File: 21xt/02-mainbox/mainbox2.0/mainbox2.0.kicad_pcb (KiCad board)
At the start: 2 copper layers, 65 parts, among them IC1 AD7175-8BCPZ-RL7, IC2 XBP9X-DMUS-011, J1 Conn_01x10, J10 Conn_02x20_Odd_Even, J3 Conn_01x06, J4 Conn_01x06, J6 Conn_01x02, J7 Conn_01x02, J9 Conn_01x06, U1 AD8222ACPZ-R7, U2 TPS78326DDCT, U3 LT6658AHMSE-2.5-PBF, U4 LT6658AHMSE-5-PBF, U5 SN74LVC245AN

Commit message: sophie needs to fix this
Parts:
- removed J6: Conn_01x02, Connector_PinHeader_2.54mm:PinHeader_1x02_P2.54mm_Vertical
- added REF**: DSUB-44-HD_Female_Horizontal_P2.29x1.98mm_EdgePinOffset3.03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, Connector_Dsub:DSUB-44-HD_Female_Horizontal_P2.29x1.98mm_EdgePinOffset3.03mm_Housed_MountingHolesOffset4.94mm, F.Cu at (20.9, 35.8)
- C1: footprint 21xt_footprints:R78B5015L - -> Capacitor_SMD:C_0603_1608Metric
- IC2: moved to B.Cu
- PS1: footprint 21xt_footprints:R78B5015L - -> 21xt_footprints:CONV_R-78B3.3-1.5
- moved C22 171.4 mm to (218.7, 71.2)
- moved C21 170.6 mm to (216.4, 97.5)
- moved C20 170.1 mm to (213.4, 98.8)
- moved C19 160.9 mm to (215.4, 73.2)
- moved C18 157.2 mm to (210.3, 84.1)
- moved C15 155.6 mm to (201.2, 84.1)
- moved C14 155.1 mm to (198.1, 84.1)
- moved C16 154.5 mm to (200.9, 69.6), turned to -90 degrees
- moved C17 151.7 mm to (201.2, 73.4)
- moved C23 151.5 mm to (202.2, 99.8)
- moved C24 145.8 mm to (199.1, 97.3)
- moved C31 140.3 mm to (183.5, 10.5), turned to 0 degrees
- moved R4 128.7 mm to (183.5, 23.2), turned to 180 degrees
- moved IC2 112.7 mm to (13.5, 135.3), turned to 180 degrees
- moved IC1 102.5 mm to (51.8, 28.2)
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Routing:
- added copper zone on F.Cu, net (none)
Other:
- copper layers 2 -> 4

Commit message: 3D modeled
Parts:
- removed REF**: DSUB-44-HD_Female_Horizontal_P2.29x1.98mm_EdgePinOffset3.03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, Connector_Dsub:DSUB-44-HD_Female_Horizontal_P2.29x1.98mm_EdgePinOffset3.03mm_Housed_MountingHolesOffset4.94mm
- moved C20 89.0 mm to (127.0, 77.4)
- moved C21 89.0 mm to (130.0, 76.1)
- moved C23 89.0 mm to (115.8, 78.4)
- moved C24 89.0 mm to (112.8, 75.9)
- moved U4 89.0 mm to (121.3, 75.7)
- moved J1 61.5 mm to (94.5, 56.9), turned to 90 degrees
- moved IC2 59.5 mm to (12.1, 75.8)
- moved C17 59.4 mm to (142.0, 68.4)
- moved C16 59.4 mm to (141.7, 64.6)
- moved C19 59.4 mm to (156.2, 68.1)
- moved C22 59.4 mm to (159.5, 66.1)
- moved U3 59.4 mm to (148.4, 66.6)
- moved J9 56.6 mm to (152.8, 48.8)
- moved J3 55.9 mm to (227.5, 41.1)
- moved C18 51.9 mm to (158.9, 77.3)
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
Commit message: progress
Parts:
- removed C11, C12, C13: 0.1uF, Capacitor_SMD:C_0603_1608Metric
- removed J4: Conn_01x06, 21xt_footprints:CONN_S6B-PH-K-S_JST (1x6)
- removed J7: Conn_01x02, Connector_PinHeader_2.54mm:PinHeader_1x02_P2.54mm_Vertical
- removed J9: Conn_01x06, 21xt_footprints:MOLEX_0533980671 (1x6)
- removed R4: 10k, Resistor_SMD:R_0603_1608Metric
- removed TP1, TP2, TP3, TP4, TP5, TP6, TP7: TestPoint, TestPoint:TestPoint_Pad_1.5x1.5mm
- removed U2: TPS78326DDCT, 21xt_footprints:TPS78326DDCT
- removed U3: LT6658AHMSE-2.5-PBF, 21xt_footprints:LT6658AHMSE-2.5-PBF
- removed U5: SN74LVC245AN, 21xt_footprints:SN74LVC245AN
- added C32: 0.1uF, Capacitor_SMD:C_0603_1608Metric, F.Cu at (100.1, 67.7)
- added C33: 3.3uF, Capacitor_SMD:C_0603_1608Metric, F.Cu at (103.1, 62.0)
- added C34: 1uF, Capacitor_SMD:C_0603_1608Metric, F.Cu at (108.4, 69.3)
- added C35: 47uF, Capacitor_SMD:C_0603_1608Metric, F.Cu at (110.2, 69.3)
- added C36: 10uF, Capacitor_SMD:C_0603_1608Metric, F.Cu at (155.6, 47.0)
- added C37: 10uF, Capacitor_SMD:C_0603_1608Metric, F.Cu at (153.7, 47.1)
- added C39: 15pF, Capacitor_SMD:C_0603_1608Metric, F.Cu at (151.7, 52.8)
- added C40: 10uF, Capacitor_SMD:C_0603_1608Metric, F.Cu at (145.5, 53.9)
- added C41: 10uF, Capacitor_SMD:C_0603_1608Metric, F.Cu at (145.5, 52.2)
- added C42: 10uF, Capacitor_SMD:C_0603_1608Metric, F.Cu at (145.5, 50.6)
- added C43: 10uF, Capacitor_SMD:C_0603_1608Metric, F.Cu at (145.5, 48.9)
- added C44: 0.1uF, Capacitor_SMD:C_0603_1608Metric, F.Cu at (133.0, 88.8)
- added C45: 0.1uF, Capacitor_SMD:C_0603_1608Metric, F.Cu at (140.3, 84.2)
- added C46: 0.1uF, Capacitor_SMD:C_0603_1608Metric, F.Cu at (140.6, 88.8)
- added IC3: TPS61088QRHLTQ1, 21xt_footprints:BQ24123RHLT, F.Cu at (104.2, 68.1)
- added IC6: AP3441LSHE-7B, 21xt_footprints:AP3441LSHE7B, F.Cu at (150.2, 48.8)
- added IC7: SN74LVC2T45DCTTG4, 21xt_footprints:SOP65P400X130-8N, F.Cu at (136.5, 84.2)
- added IC8: SN74LVC2T45DCTTG4, 21xt_footprints:SOP65P400X130-8N, F.Cu at (136.8, 88.8)
- added J2: Conn_01x10, 21xt_footprints:908160010(picolex-10), F.Cu at (91.5, 68.7)
- added J5: MDT275M02001, 21xt_footprints:AMPHENOL_MDT275M02001, F.Cu at (155.2, 69.1)
- added J6: Conn_01x02, 21xt_footprints:JST_B2P-VH_LF__SN_(2 pin), F.Cu at (95.2, 47.2)
- added L2: 22uH, Inductor_SMD:L_0402_1005Metric, F.Cu at (148.4, 45.1)
- added L3: 1.2uH, Inductor_SMD:L_0402_1005Metric, F.Cu at (98.5, 67.7)
- added Q1: DMG1012T-7, 21xt_footprints:SOT50P160X90-3N(DIODE), F.Cu at (160.6, 61.9)
- added R10: 33, Resistor_SMD:R_0603_1608Metric, F.Cu at (160.6, 66.2)
- added R11: 10k, Resistor_SMD:R_0603_1608Metric, F.Cu at (149.1, 52.8)
- added R12: 22k, Resistor_SMD:R_0603_1608Metric, F.Cu at (155.0, 51.6)
- added R13: 290k, Resistor_SMD:R_0603_1608Metric, F.Cu at (110.1, 66.1)
- added R14: 56k, Resistor_SMD:R_0603_1608Metric, F.Cu at (112.5, 64.1)
- added R15: 100k, Resistor_SMD:R_0603_1608Metric, F.Cu at (160.5, 69.9)
- added R16: 60k, Resistor_SMD:R_0603_1608Metric, F.Cu at (108.3, 66.2)
- added R17: 10k, Resistor_SMD:R_0603_1608Metric, F.Cu at (157.6, 49.6)
- C1, C10, C14: value 1uF -> 0.1uF
- C18: value 2.2uF -> 0.6nF
- C19: value 0.1uF -> 3.1pF
- C2, C8: value 10uF -> 1uF
- C22: value 1uF -> 47nF
- C25, C28, C29, C30, PS1: moved to B.Cu
- C26: value 4.7 -> 4.7uF; moved to B.Cu
- C27: value 0.1 -> 0.1uF; moved to B.Cu
- C4: value 0.1uF -> 1uF
- C5: value 10uF -> 0.1uF
- C6, C9: value 0.1uF -> 10uF
- H1, H2, H3, H4: footprint 21xt_footprints:2.35mm_mounting_hole -> MountingHole:MountingHole_2.5mm
- IC1: value AD7175-8BCPZ-RL7 -> SN74LVC2T45DCTTG4; footprint 21xt_footprints:QFN50P600X600X80-41N-D -> 21xt_footprints:SOP65P400X130-8N
- J1: footprint 21xt_footprints:MOLEX_533981071 (1x10) -> 21xt_footprints:908160010(picolex-10)
- J3: value Conn_01x06 -> Conn_01x16; footprint 21xt_footprints:MOLEX_0533980671 (1x6) -> 21xt_footprints:SAMTEC_ZF5S-16-01-T-WT
- R1: value 10k -> 225k
- R2: value 200 -> 49.9k
- R3: value 200 -> 125k
- U1: value AD8222ACPZ-R7 -> AD7175-2BRUZ; footprint 21xt_footprints:AD8222ACPZ-R7 -> 21xt_footprints:RU_24_ADI
- moved IC1 119.3 mm to (150.7, 87.9), turned to 0 degrees
- moved R5 117.5 mm to (162.4, 88.7)
- moved R6 113.1 mm to (160.2, 88.7), turned to -90 degrees
- moved R7 110.5 mm to (157.3, 84.0), turned to 0 degrees
- moved PS1 104.9 mm to (122.7, 50.0), turned to 180 degrees
- moved C31 103.3 mm to (100.2, 71.5), turned to -90 degrees
- moved C3 102.4 mm to (125.2, 84.4), turned to -90 degrees
- moved C4 101.7 mm to (126.8, 84.3), turned to -90 degrees
- moved C5 101.1 mm to (125.5, 87.6), turned to -90 degrees
- moved C6 101.0 mm to (127.1, 87.6), turned to -90 degrees
- moved C1 95.9 mm to (114.2, 84.8), turned to -90 degrees
- moved L1 95.5 mm to (131.6, 48.8)
- moved C2 91.5 mm to (111.4, 84.8), turned to -90 degrees
- moved C25 86.2 mm to (120.4, 76.5), turned to 180 degrees
- moved C26 85.5 mm to (120.4, 74.4), turned to 180 degrees
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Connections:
- C1 pad 1: GND -> Net-(U1-REGCAPA)
- C1 pad 2: Net-(IC1-REGCAPA) -> GND
- C10 pad 1: Net-(IC1-REGCAPD) -> GND
- C10 pad 2: GND -> 5VRef
- C14 pad 2: 5.2V -> 3V3
- C16 pad 2: Net-(U3-BYPASS) -> 3V3
- C17 pad 1: GND -> Vin
- C17 pad 2: Net-(U3-NR) -> GND
- C18 pad 1: GND -> Net-(C18-Pad1)
- C18 pad 2: 5VADC -> GND
- C19 pad 1: 5VADC -> Net-(IC3-COMP)
- C2 pad 1: 5VADC -> Net-(U1-REGCAPA)
- C22 pad 1: GND -> Net-(IC3-SS)
- C22 pad 2: 2.5V -> GND
- C23 pad 1: 5.2V -> 7.5VBOOST
- C24 pad 2: 5VASupply/Ref -> 5VRef
- C27 pad 2: VOUT -> 3V3_XBEE
- C28 pad 2: VOUT -> 3V3_XBEE
- C29 pad 2: VOUT -> 3V3_XBEE
- C3 pad 2: Net-(IC1-REGCAPA) -> Net-(U1-REGCAPD)
- C30 pad 2: VOUT -> 3V3_XBEE
- C31 pad 1: GND -> Vin
- C31 pad 2: 3V3 -> GND
- C4 pad 1: 5VADC -> GND
- C4 pad 2: GND -> Net-(U1-REGCAPD)
- C5 pad 1: 5VASupply/Ref -> 3V3
- C6 pad 1: 5VASupply/Ref -> 3V3
- C7 pad 1: 3V3 -> GND
- C7 pad 2: GND -> 5VADC/SENSOR
- C8 pad 1: 3V3 -> GND
- C8 pad 2: GND -> 5VADC/SENSOR
- C9 pad 1: Net-(IC1-REGCAPD) -> GND
- C9 pad 2: GND -> 5VRef
- IC1 pad 1: ANI16 -> 5.2V
- IC1 pad 2: GND -> IN1(5V)
- IC1 pad 3: ANI1 -> IN2(5V)
- IC1 pad 5: ANI3 -> GND
- IC1 pad 6: unconnected-(IC1-REFOUT-Pad6) -> IN2(3.3V)
- IC1 pad 7: Net-(IC1-REGCAPA) -> IN1(3.3V)
- IC1 pad 8: GND -> 3V3
- IC2 pad 11: unconnected-(IC2-GND_2-Pad11) -> GND
- IC2 pad 13: unconnected-(IC2-GND_3-Pad13) -> GND
- IC2 pad 2: VOUT -> 3V3_XBEE
- IC2 pad 22: unconnected-(IC2-GND_4-Pad22) -> GND
- IC2 pad 35: unconnected-(IC2-GND_5-Pad35) -> GND
- J1 pad 1: 5VASupply/Ref -> NAVOUT
- J1 pad 10: ANI3 -> IN2(5V)
- J1 pad 2: GND -> NAVIN
- J1 pad 3: ANI9 -> POWER_BOARD_TX
- J1 pad 4: ANI11 -> POWER_BOARD_RX
- J1 pad 5: ANI13 -> STEERING_WHEEL_TX
- J1 pad 6: ANI14 -> STEERING_WHEEL_RX
- J1 pad 7: ANI15 -> 5.2V
- J1 pad 8: ANI1 -> GND
- J1 pad 9: ANI16 -> IN1(5V)
- J10 pad 11: DO4 -> IN1(3.3V)
- J10 pad 13: DO5 -> IN2(3.3V)
- J10 pad 15: DO6 -> unconnected-(J10-Pin_15-Pad15)
- J10 pad 27: unconnected-(J10-Pin_27-Pad27) -> STEERING_WHEEL_TX
- J10 pad 29: unconnected-(J10-Pin_29-Pad29) -> STEERING_WHEEL_RX
- J10 pad 3: DO1 -> DIGITAL_OUTPUT_1
- J10 pad 5: DO2 -> DIGITAL_OUTPUT_2
- J10 pad 7: DO3 -> unconnected-(J10-Pin_7-Pad7)
- PS1 pad 3: VOUT -> 3V3_XBEE
- R1 pad 1: 3V3 -> Net-(IC3-SW_1)
- R1 pad 2: Net-(IC1-~{ERROR}) -> Net-(IC3-FSW)
- R2 pad 1: Net-(U1-RG1__1) -> GND
- R2 pad 2: Net-(U1-RG1) -> Net-(IC3-ILIM)
- R3 pad 1: Net-(U1-RG2__1) -> Net-(IC3-COMP)
- R3 pad 2: Net-(U1-RG2) -> Net-(C18-Pad1)
- U1 pad 1: SG1- -> ANI4
- U1 pad 10: Net-(U1-RG2) -> unconnected-(U1-XTAL2/CLKIO-Pad10)
- U1 pad 11: Net-(U1-RG2__1) -> DOUT
- U1 pad 12: SG2- -> DIN
- U1 pad 13: GND -> SCLK
- U1 pad 14: SG2 -> CS
- U1 pad 15: SG1 -> GND
- U1 pad 16: 5VADC -> 3V3
- U1 pad 2: Net-(U1-RG1) -> GND
- U1 pad 3: Net-(U1-RG1__1) -> 5VRef
- U1 pad 4: SG1+ -> unconnected-(U1-REFOUT-Pad4)
- U1 pad 5: 5VADC -> Net-(U1-REGCAPA)
- U1 pad 6: 2.5V -> GND
- U1 pad 7: 2.5V -> 5VADC/SENSOR
- U1 pad 8: GND -> 5VADC/SENSOR
- U1 pad 9: SG2+ -> unconnected-(U1-XTAL1-Pad9)
- U4 pad 10: 5.2V -> 7.5VBOOST
- U4 pad 11: 5.2V -> 7.5VBOOST
- U4 pad 12: 5VASupply/Ref -> 5VRef
- U4 pad 13: 5VASupply/Ref -> 5VRef
- U4 pad 14: 5.2V -> 7.5VBOOST
- U4 pad 7: 5VASupply/Ref -> 5VADC/SENSOR
- U4 pad 8: 5VASupply/Ref -> 5VADC/SENSOR
- U4 pad 9: 5.2V -> 7.5VBOOST
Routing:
- added copper zone on B.Cu, net (none)
- added copper zone on In2.Cu, net 5.2V
- added copper zone on In1.Cu, net GND
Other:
- board text added: "Incorrect foorprint"
- board text added: "Messed up footprint - will fix"
- board text added: "Not accurate component"
- board text added: "need hole for SSD!!"

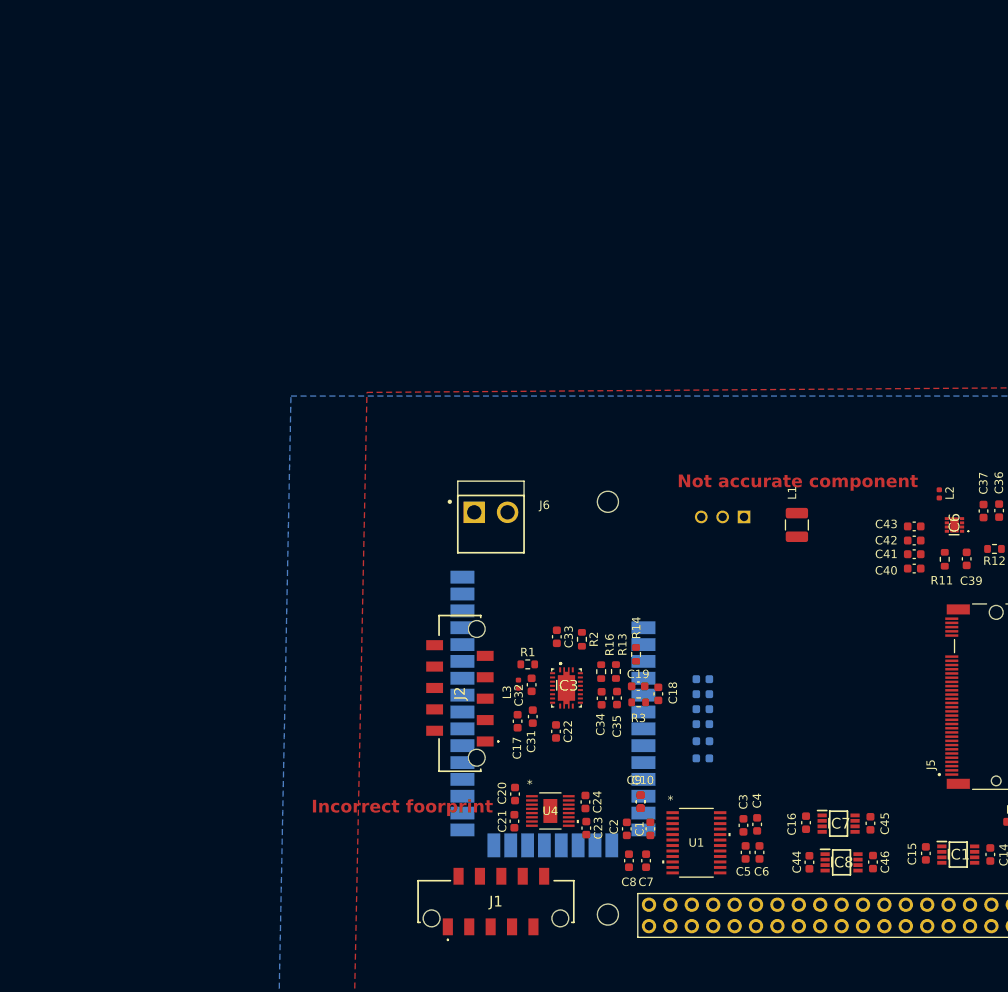
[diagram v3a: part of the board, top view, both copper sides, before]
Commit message: shift SSD
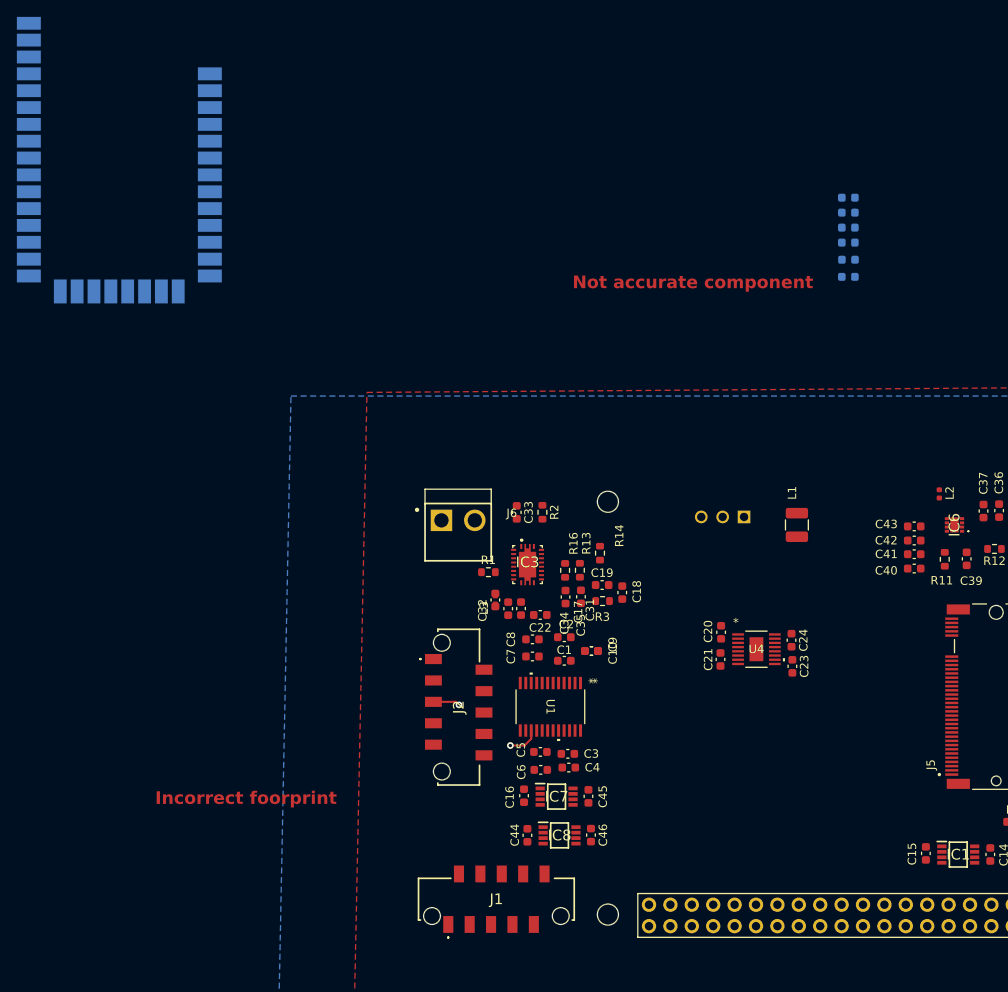
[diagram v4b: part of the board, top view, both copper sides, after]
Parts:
- moved IC2 83.5 mm to (40.1, 21.3)
- moved C29 59.7 mm to (137.7, 11.7)
- moved C26 59.7 mm to (137.7, 17.3)
- moved C27 59.7 mm to (137.7, 15.2)
- moved C30 59.7 mm to (137.7, 9.91)
- moved C25 59.7 mm to (137.7, 19.3)
- moved C28 59.7 mm to (137.7, 13.5)
- moved C46 33.6 mm to (107.1, 85.6)
- moved C16 33.6 mm to (99.2, 80.9)
- moved C44 33.6 mm to (99.6, 85.6)
- moved C45 33.6 mm to (106.8, 81.0)
- moved IC7 33.6 mm to (103.0, 81.0)
- moved IC8 33.6 mm to (103.4, 85.6)
- moved C23 31.1 mm to (131.0, 65.5)
- moved C20 31.1 mm to (122.6, 61.5)
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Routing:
- net GND: track 0.00 -> 6.97 mm, vias 0 -> 2
